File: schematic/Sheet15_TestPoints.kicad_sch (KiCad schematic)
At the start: 16 parts

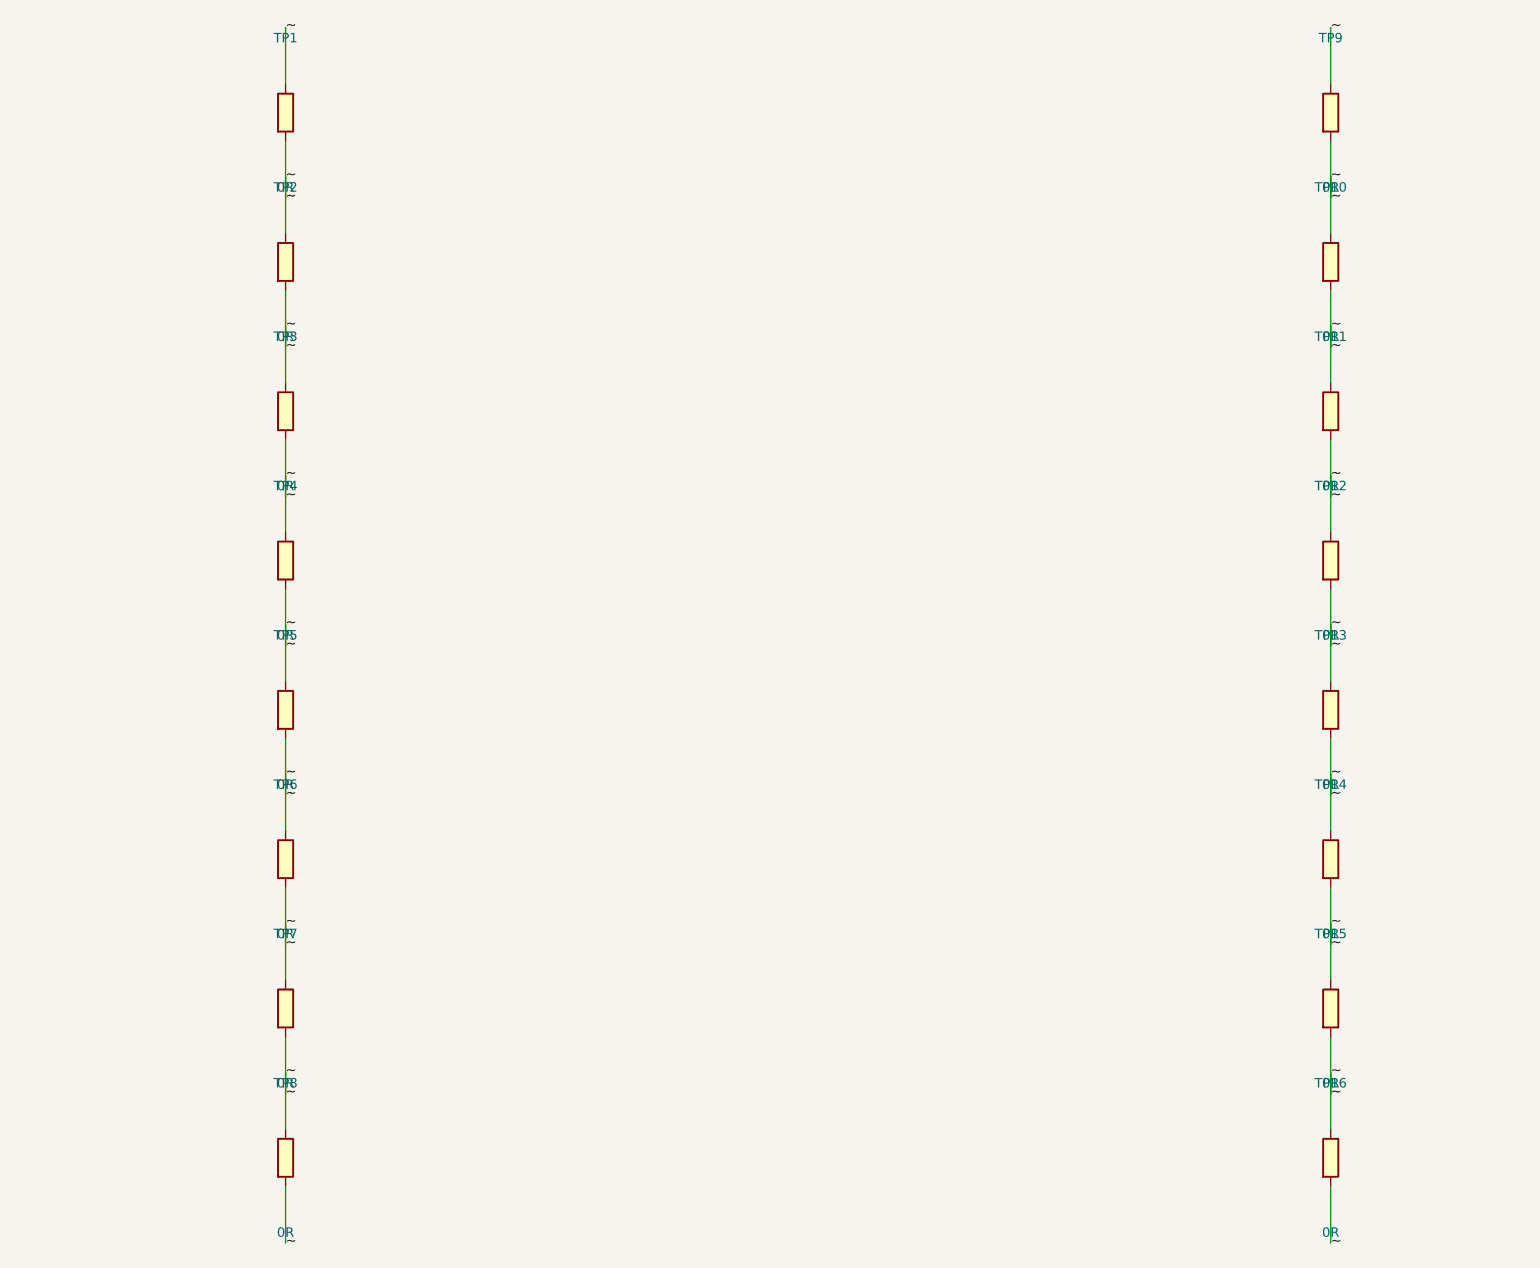
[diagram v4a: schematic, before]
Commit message: fix: isolate ISL70003ASEH buck pins, fix LMX_SYNC collision, NC pins, connector pin names
- ISL70003ASEH pins now use ref prefix (U6_LX1 vs U7_LX1) to prevent shorts
- Buck SYNC pins separated from LMX_SYNC (power sync ≠ PLL sync)
- NC pins properly skipped (unconnected)
- Connector PIN_1..PIN_6 use ref prefix (J1_PIN_1 vs J2_PIN_1)
- Fixed annotation warnings in Sheet13 (C_dev→C125, R_dev→R74, U_TPS7H→U14)
- Regenerated all PDFs and SVGs
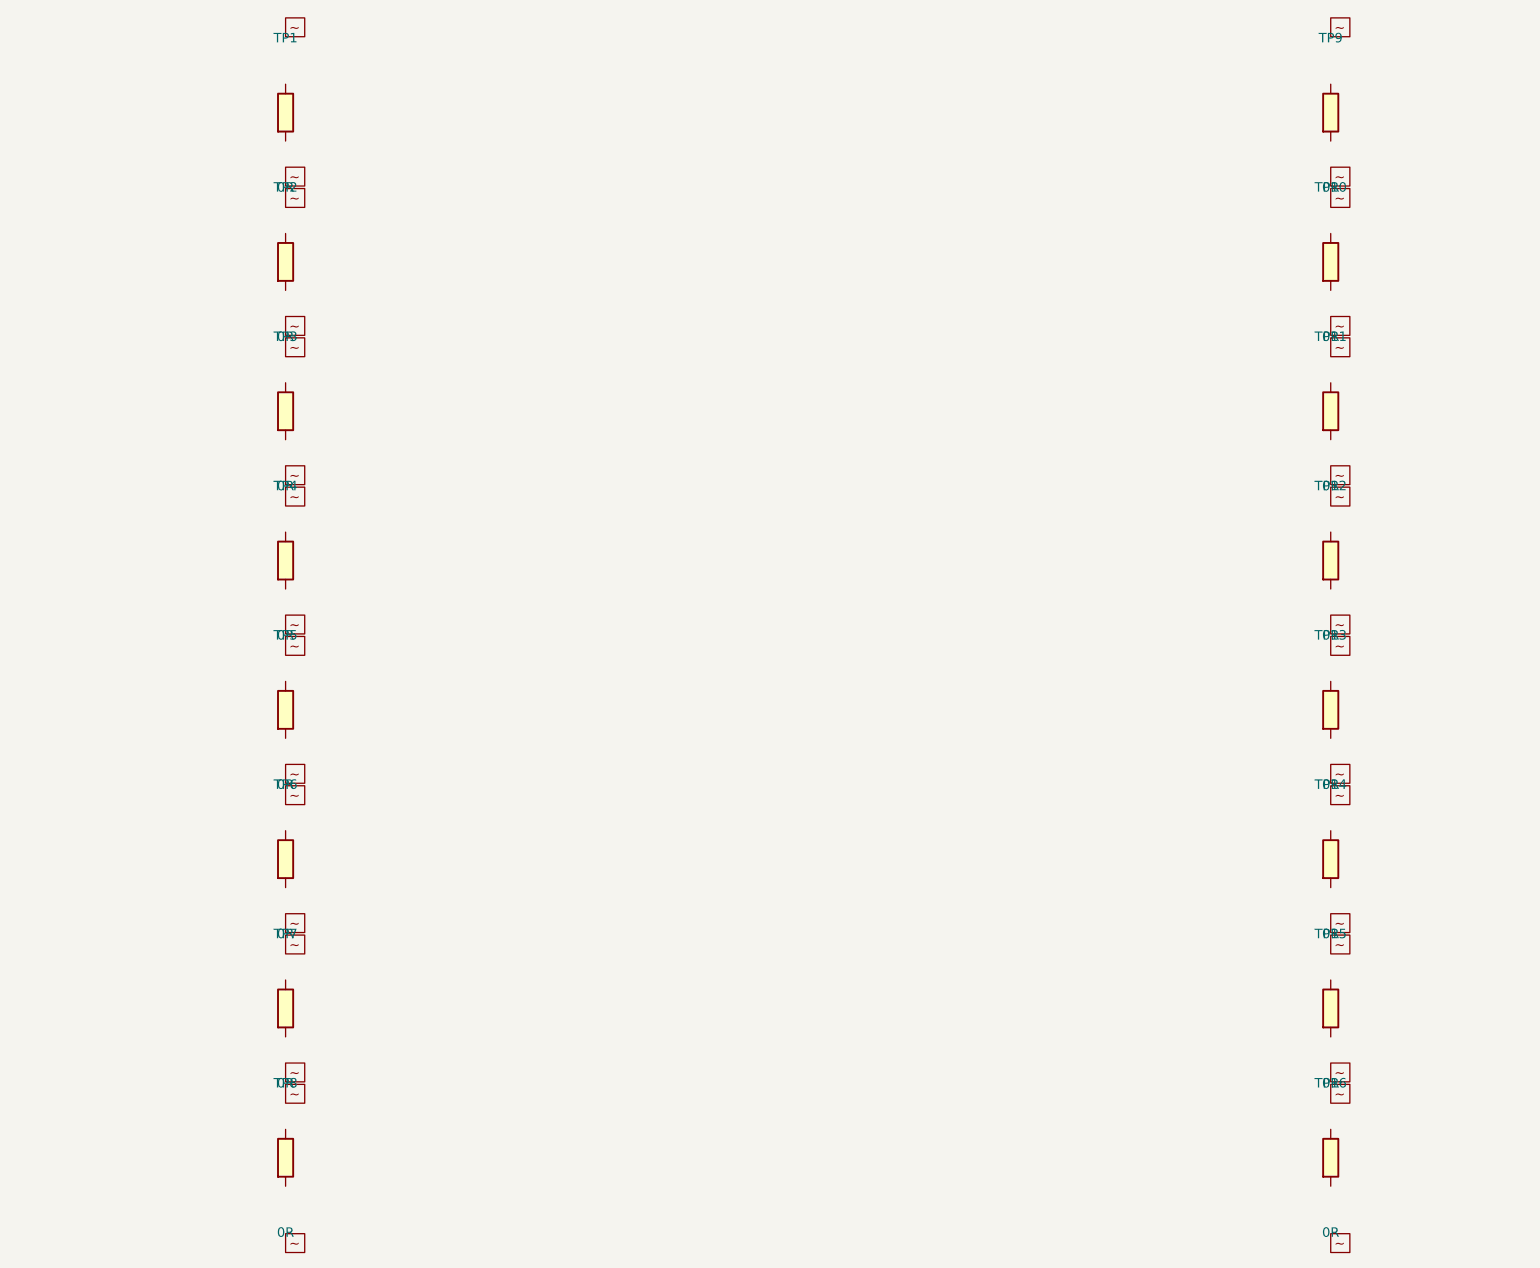
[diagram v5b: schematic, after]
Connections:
- net ~: no longer TP1.1, TP1.2, TP10.1, TP10.2, TP11.1, TP11.2, TP12.1, TP12.2, TP13.1, TP13.2, TP14.1, TP14.2, TP15.1, TP15.2, TP16.1, TP16.2, TP2.1, TP2.2, TP3.1, TP3.2, TP4.1, TP4.2, TP5.1, TP5.2, TP6.1, TP6.2, TP7.1, TP7.2, TP8.1, TP8.2, TP9.1, TP9.2
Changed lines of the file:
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@@
     (pin "2")
   )
-  (wire (pts (xy 60.0000 36.1900) (xy 60.0000 28.5700)) (stroke (width 0) (type default)))
-  (label "~" (at 60.0000 28.5700 0) (effects (font (size 1.27 1.27))))
-  (wire (pts (xy 60.0000 43.8100) (xy 60.0000 51.4300)) (stroke (width 0) (type default)))
-  (label "~" (at 60.0000 51.4300 0) (effects (font (size 1.27 1.27))))
-  (wire (pts (xy 60.0000 56.1900) (xy 60.0000 48.5700)) (stroke (width 0) (type default)))
-  (label "~" (at 60.0000 48.5700 0) (effects (font (size 1.27 1.27))))
-  (wire (pts (xy 60.0000 63.8100) (xy 60.0000 71.4300)) (stroke (width 0) (type default)))
-  (label "~" (at 60.0000 71.4300 0) (effects (font (size 1.27 1.27))))
-  (wire (pts (xy 60.0000 76.1900) (xy 60.0000 68.5700)) (stroke (width 0) (type default)))
-  (label "~" (at 60.0000 68.5700 0) (effects (font (size 1.27 1.27))))
-  (wire (pts (xy 60.0000 83.8100) (xy 60.0000 91.4300)) (stroke (width 0) (type default)))
-  (label "~" (at 60.0000 91.4300 0) (effects (font (size 1.27 1.27))))
-  (wire (pts (xy 60.0000 96.1900) (xy 60.0000 88.5700)) (stroke (width 0) (type default)))
-  (label "~" (at 60.0000 88.5700 0) (effects (font (size 1.27 1.27))))
-  (wire (pts (xy 60.0000 103.8100) (xy 60.0000 111.4300)) (stroke (width 0) (type default)))
-  (label "~" (at 60.0000 111.4300 0) (effects (font (size 1.27 1.27))))
-  (wire (pts (xy 60.0000 116.1900) (xy 60.0000 108.5700)) (stroke (width 0) (type default)))
-  (label "~" (at 60.0000 108.5700 0) (effects (font (size 1.27 1.27))))
-  (wire (pts (xy 60.0000 123.8100) (xy 60.0000 131.4300)) (stroke (width 0) (type default)))
-  (label "~" (at 60.0000 131.4300 0) (effects (font (size 1.27 1.27))))
-  (wire (pts (xy 60.0000 136.1900) (xy 60.0000 128.5700)) (stroke (width 0) (type default)))
-  (label "~" (at 60.0000 128.5700 0) (effects (font (size 1.27 1.27))))
-  (wire (pts (xy 60.0000 143.8100) (xy 60.0000 151.4300)) (stroke (width 0) (type default)))
-  (label "~" (at 60.0000 151.4300 0) (effects (font (size 1.27 1.27))))
-  (wire (pts (xy 60.0000 156.1900) (xy 60.0000 148.5700)) (stroke (width 0) (type default)))
-  (label "~" (at 60.0000 148.5700 0) (effects (font (size 1.27 1.27))))
-  (wire (pts (xy 60.0000 163.8100) (xy 60.0000 171.4300)) (stroke (width 0) (type default)))
-  (label "~" (at 60.0000 171.4300 0) (effects (font (size 1.27 1.27))))
-  (wire (pts (xy 60.0000 176.1900) (xy 60.0000 168.5700)) (stroke (width 0) (type default)))
-  (label "~" (at 60.0000 168.5700 0) (effects (font (size 1.27 1.27))))
-  (wire (pts (xy 60.0000 183.8100) (xy 60.0000 191.4300)) (stroke (width 0) (type default)))
-  (label "~" (at 60.0000 191.4300 0) (effects (font (size 1.27 1.27))))
-  (wire (pts (xy 200.0000 36.1900) (xy 200.0000 28.5700)) (stroke (width 0) (type default)))
-  (label "~" (at 200.0000 28.5700 0) (effects (font (size 1.27 1.27))))
-  (wire (pts (xy 200.0000 43.8100) (xy 200.0000 51.4300)) (stroke (width 0) (type default)))
-  (label "~" (at 200.0000 51.4300 0) (effects (font (size 1.27 1.27))))
-  (wire (pts (xy 200.0000 56.1900) (xy 200.0000 48.5700)) (stroke (width 0) (type default)))
-  (label "~" (at 200.0000 48.5700 0) (effects (font (size 1.27 1.27))))
-  (wire (pts (xy 200.0000 63.8100) (xy 200.0000 71.4300)) (stroke (width 0) (type default)))
-  (label "~" (at 200.0000 71.4300 0) (effects (font (size 1.27 1.27))))
-  (wire (pts (xy 200.0000 76.1900) (xy 200.0000 68.5700)) (stroke (width 0) (type default)))
-  (label "~" (at 200.0000 68.5700 0) (effects (font (size 1.27 1.27))))
-  (wire (pts (xy 200.0000 83.8100) (xy 200.0000 91.4300)) (stroke (width 0) (type default)))
-  (label "~" (at 200.0000 91.4300 0) (effects (font (size 1.27 1.27))))
-  (wire (pts (xy 200.0000 96.1900) (xy 200.0000 88.5700)) (stroke (width 0) (type default)))
-  (label "~" (at 200.0000 88.5700 0) (effects (font (size 1.27 1.27))))
-  (wire (pts (xy 200.0000 103.8100) (xy 200.0000 111.4300)) (stroke (width 0) (type default)))
-  (label "~" (at 200.0000 111.4300 0) (effects (font (size 1.27 1.27))))
-  (wire (pts (xy 200.0000 116.1900) (xy 200.0000 108.5700)) (stroke (width 0) (type default)))
-  (label "~" (at 200.0000 108.5700 0) (effects (font (size 1.27 1.27))))
-  (wire (pts (xy 200.0000 123.8100) (xy 200.0000 131.4300)) (stroke (width 0) (type default)))
-  (label "~" (at 200.0000 131.4300 0) (effects (font (size 1.27 1.27))))
-  (wire (pts (xy 200.0000 136.1900) (xy 200.0000 128.5700)) (stroke (width 0) (type default)))
-  (label "~" (at 200.0000 128.5700 0) (effects (font (size 1.27 1.27))))
-  (wire (pts (xy 200.0000 143.8100) (xy 200.0000 151.4300)) (stroke (width 0) (type default)))
-  (label "~" (at 200.0000 151.4300 0) (effects (font (size 1.27 1.27))))
-  (wire (pts (xy 200.0000 156.1900) (xy 200.0000 148.5700)) (stroke (width 0) (type default)))
-  (label "~" (at 200.0000 148.5700 0) (effects (font (size 1.27 1.27))))
-  (wire (pts (xy 200.0000 163.8100) (xy 200.0000 171.4300)) (stroke (width 0) (type default)))
-  (label "~" (at 200.0000 171.4300 0) (effects (font (size 1.27 1.27))))
-  (wire (pts (xy 200.0000 176.1900) (xy 200.0000 168.5700)) (stroke (width 0) (type default)))
-  (label "~" (at 200.0000 168.5700 0) (effects (font (size 1.27 1.27))))
-  (wire (pts (xy 200.0000 183.8100) (xy 200.0000 191.4300)) (stroke (width 0) (type default)))
-  (label "~" (at 200.0000 191.4300 0) (effects (font (size 1.27 1.27))))
+  (global_label "~" (at 60.0000 28.5700 0) (effects (font (size 1.27 1.27))))
+  (global_label "~" (at 60.0000 51.4300 0) (effects (font (size 1.27 1.27))))
+  (global_label "~" (at 60.0000 48.5700 0) (effects (font (size 1.27 1.27))))
+  (global_label "~" (at 60.0000 71.4300 0) (effects (font (size 1.27 1.27))))
+  (global_label "~" (at 60.0000 68.5700 0) (effects (font (size 1.27 1.27))))
+  (global_label "~" (at 60.0000 91.4300 0) (effects (font (size 1.27 1.27))))
+  (global_label "~" (at 60.0000 88.5700 0) (effects (font (size 1.27 1.27))))
+  (global_label "~" (at 60.0000 111.4300 0) (effects (font (size 1.27 1.27))))
+  (global_label "~" (at 60.0000 108.5700 0) (effects (font (size 1.27 1.27))))
+  (global_label "~" (at 60.0000 131.4300 0) (effects (font (size 1.27 1.27))))
+  (global_label "~" (at 60.0000 128.5700 0) (effects (font (size 1.27 1.27))))
+  (global_label "~" (at 60.0000 151.4300 0) (effects (font (size 1.27 1.27))))
+  (global_label "~" (at 60.0000 148.5700 0) (effects (font (size 1.27 1.27))))
+  (global_label "~" (at 60.0000 171.4300 0) (effects (font (size 1.27 1.27))))
+  (global_label "~" (at 60.0000 168.5700 0) (effects (font (size 1.27 1.27))))
+  (global_label "~" (at 60.0000 191.4300 0) (effects (font (size 1.27 1.27))))
+  (global_label "~" (at 200.0000 28.5700 0) (effects (font (size 1.27 1.27))))
+  (global_label "~" (at 200.0000 51.4300 0) (effects (font (size 1.27 1.27))))
+  (global_label "~" (at 200.0000 48.5700 0) (effects (font (size 1.27 1.27))))
+  (global_label "~" (at 200.0000 71.4300 0) (effects (font (size 1.27 1.27))))
+  (global_label "~" (at 200.0000 68.5700 0) (effects (font (size 1.27 1.27))))
+  (global_label "~" (at 200.0000 91.4300 0) (effects (font (size 1.27 1.27))))
+  (global_label "~" (at 200.0000 88.5700 0) (effects (font (size 1.27 1.27))))
+  (global_label "~" (at 200.0000 111.4300 0) (effects (font (size 1.27 1.27))))
+  (global_label "~" (at 200.0000 108.5700 0) (effects (font (size 1.27 1.27))))
+  (global_label "~" (at 200.0000 131.4300 0) (effects (font (size 1.27 1.27))))
+  (global_label "~" (at 200.0000 128.5700 0) (effects (font (size 1.27 1.27))))
+  (global_label "~" (at 200.0000 151.4300 0) (effects (font (size 1.27 1.27))))
+  (global_label "~" (at 200.0000 148.5700 0) (effects (font (size 1.27 1.27))))
+  (global_label "~" (at 200.0000 171.4300 0) (effects (font (size 1.27 1.27))))
+  (global_label "~" (at 200.0000 168.5700 0) (effects (font (size 1.27 1.27))))
+  (global_label "~" (at 200.0000 191.4300 0) (effects (font (size 1.27 1.27))))
   (sheet_instances (path "/" (page "1")))
 )
